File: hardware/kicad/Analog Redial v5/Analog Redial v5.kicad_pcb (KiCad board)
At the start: 2 copper layers, 115 x 52 mm, 76 parts, among them J1 Barrel_Jack_PTH_Slot, J2 PINHD_1x8_Male, J3 PINHD_1x2_Male, J4 PINHD_1x2_Male, J5 PINHD_2x4_Male, J7 PINHD_1x3_Male, J8 RJ12, J9 RJ12, U1 ESP32-C6-DevKitC-1, U2 ES8388, U3 AG1171, U4 AG1171, U5 XC6206PxxxMR

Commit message: v5 board: one set of files, named 'Analog Redial v5'
The Oct 7 working copy (was 'Analog Redial 5.*') becomes
'Analog Redial v5.*', matching v2/v4/v6 and the doc paths. Project name,
schematic instance paths and PCB sheetfile references renamed to match;
the silkscreen texts are untouched. The old as-fabbed v5 pcb, fab zip
and stale project file are removed here and remain in d18d89c.

Checked after the rename: netlist has the same 75 parts and 91 nets,
DRC reports 0 violations / 0 unconnected / 0 footprint errors.

Co-Authored-By: Claude Sonnet 5.5 <noreply@anthropic.com>
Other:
- board text added: "Analog Redial 5"
- board text removed: "Analog Redial v5"

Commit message: KiCad v5: edits as of 2026-10-19
Co-Authored-By: Claude Opus 5.5 <noreply@anthropic.com>
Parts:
- removed REF**: OSHW-Logo2_14.6x12mm_SilkScreen, Symbol:OSHW-Logo2_14.6x12mm_SilkScreen
- U5: value XC6206PxxxMR -> XC6206P332MR

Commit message: v5 PCB: clone 5V pin footprint fixed; docs say the warning is for boards made before the fix
Co-Authored-By: Claude Sonnet 5.5 <noreply@anthropic.com>
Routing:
- net +5V: track 147.9 -> 182.8 mm

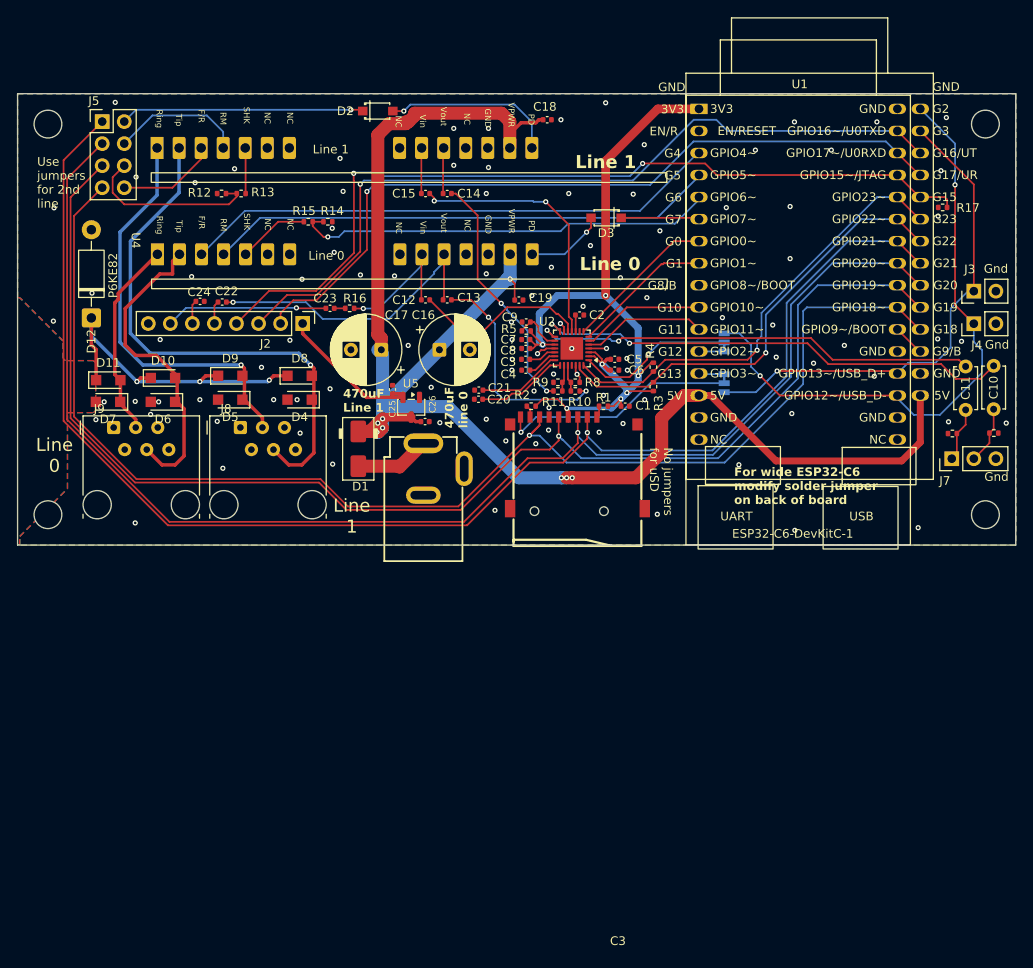
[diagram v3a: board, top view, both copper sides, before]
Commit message: v5 back to the as-fabbed files; v5.1 = v5 with the clone 5V-pin fix; track every board's JLCPCB/PCBWay exports. Docs: expansion header (J2) with its pinout, payphone section. Echo test: quiet the line before measuring (dial tone hid the echo). Wi-Fi power-save allowed with board-to-board numbers
Co-Authored-By: Claude Opus 5.5 <noreply@anthropic.com>
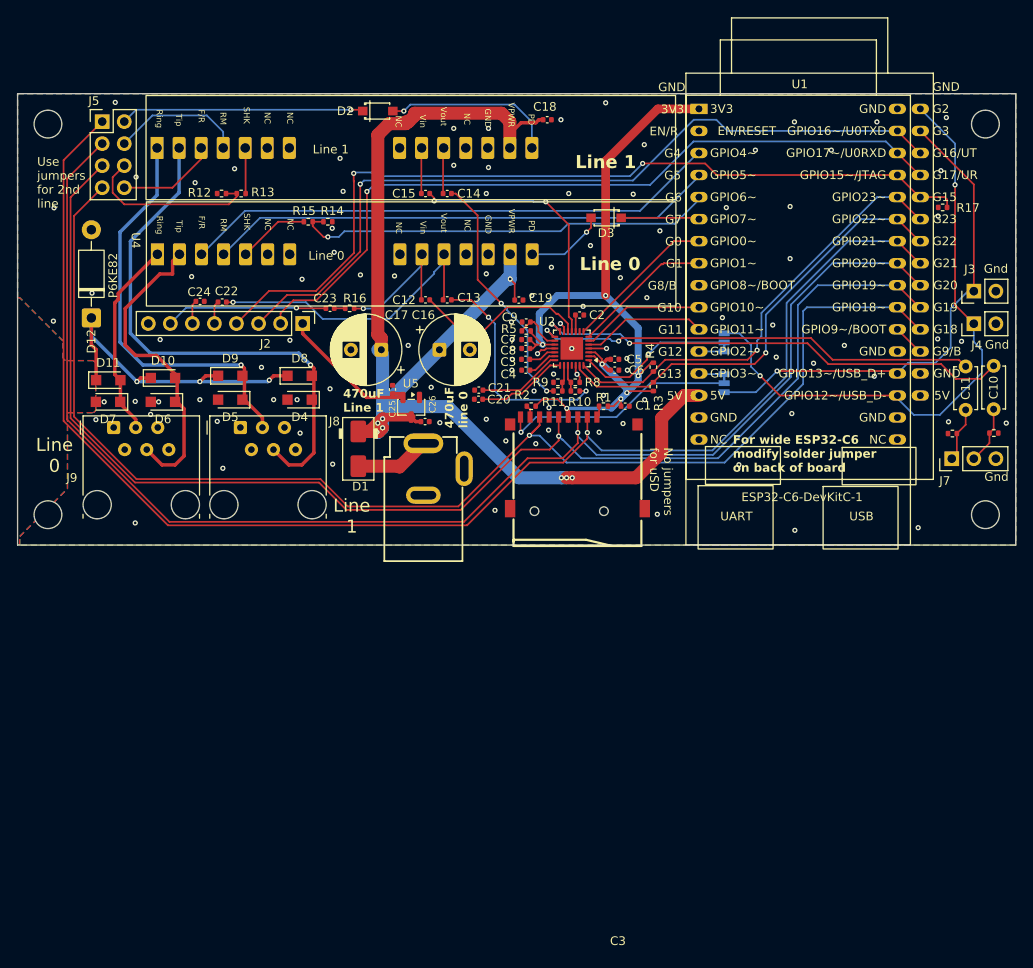
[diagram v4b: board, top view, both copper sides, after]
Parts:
- added REF**: OSHW-Logo2_14.6x12mm_SilkScreen, Symbol:OSHW-Logo2_14.6x12mm_SilkScreen, B.Cu at (87.9, 60.7)
- U5: value XC6206P332MR -> XC6206PxxxMR
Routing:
- net +5V: track 182.8 -> 147.9 mm
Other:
- board text added: "Analog Redial v5"
- board text removed: "Analog Redial 5"
